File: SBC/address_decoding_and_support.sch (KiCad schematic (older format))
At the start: 15 parts, among them Q1 DS1813, SW1 RESET, SW2 PANIC, U5 TL7705B, U6 PlutoDecoder, U8 74HC74, X1 8MHz

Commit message: New PCB layout is taking shape.
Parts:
- removed RN1: 3.3k, Resistor_SMD:R_Array_Convex_8x0602, symbol Device:R_Network08
- added RN1: 3.3k, Resistor_SMD:R_Array_Convex_5x1206, symbol Grotto:R_Network08_SMD
- C10, C6, C9: footprint Capacitor_SMD:C_0603_1608Metric_Pad1.05x0.95mm_HandSolder -> Capacitor_SMD:C_0805_2012Metric_Pad1.15x1.40mm_HandSolder
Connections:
- net BE: now also RN1.7 (R6)
- net RDY: now also RN1.4 (R4)
- net VCC: now also RN1.10 (common), RN1.5 (common)
- net ~IRQ: now also RN1.9 (R8)
- net ~KS: now also RN1.2 (R2)
- net ~NMI: now also RN1.8 (R7)
- net ~PWR: now also RN1.6 (R5)
- net ~RES: now also RN1.1 (R1)
- net ~SO: now also RN1.3 (R3)
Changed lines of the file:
@@
 F 0 "C6" H 3650 3700 50  0000 L CNN
 F 1 "0.1uF" H 3425 3550 50  0000 L CNN
-F 2 "Capacitor_SMD:C_0603_1608Metric_Pad1.05x0.95mm_HandSolder" H 3650 3625 50  0001 C CNN
+F 2 "Capacitor_SMD:C_0805_2012Metric_Pad1.15x1.40mm_HandSolder" H 3650 3625 50  0001 C CNN
 F 3 "" H 3650 3625 50  0001 C CNN
 	1    3650 3625
@@
 	4350 1800 4675 1800
 Wire Wire Line
-	3650 1200 3650 1025
-Wire Wire Line
 	4650 6450 4900 6450
 Wire Wire Line
@@
 Wire Wire Line
 	3750 2400 4675 2400
-$Comp
-L Device:R_Network08 RN1
-U 1 1 5D76ADD1
-P 4050 1400
-F 0 "RN1" V 3550 1325 50  0000 L CNN
-F 1 "3.3k" V 4450 1300 50  0000 L CNN
-F 2 "Resistor_SMD:R_Array_Convex_8x0602" V 4525 1400 50  0001 C CNN
-F 3 "http://www.vishay.com/docs/31509/csc.pdf" H 4050 1400 50  0001 C CNN
-	1    4050 1400
-	1    0    0    -1
-$EndComp
 Wire Wire Line
 	4675 2500 3650 2500
@@
 F 0 "C9" V 8775 800 50  0000 C CNN
 F 1 "0.1uF" V 9025 800 50  0000 C CNN
-F 2 "Capacitor_SMD:C_0603_1608Metric_Pad1.05x0.95mm_HandSolder" H 8900 800 50  0001 C CNN
+F 2 "Capacitor_SMD:C_0805_2012Metric_Pad1.15x1.40mm_HandSolder" H 8900 800 50  0001 C CNN
 F 3 "~" H 8900 800 50  0001 C CNN
 	1    8900 800
@@
 F 0 "C10" V 3775 6775 50  0000 L CNN
 F 1 "0.1uF" V 4000 6750 50  0000 L CNN
-F 2 "Capacitor_SMD:C_0603_1608Metric_Pad1.05x0.95mm_HandSolder" H 3875 6825 50  0001 C CNN
+F 2 "Capacitor_SMD:C_0805_2012Metric_Pad1.15x1.40mm_HandSolder" H 3875 6825 50  0001 C CNN
 F 3 "" H 3875 6825 50  0001 C CNN
 	1    3875 6825
@@
 	3775 6150 4050 6150
 Connection ~ 4050 6150
+$Comp
+L Grotto:R_Network08_SMD RN1
+U 1 1 5D847681
+P 4050 1400
+F 0 "RN1" V 3550 1325 50  0000 L CNN
+F 1 "3.3k" V 4450 1325 50  0000 L CNN
+F 2 "Resistor_SMD:R_Array_Convex_5x1206" V 4525 1400 50  0001 C CNN
+F 3 "https://industrial.panasonic.com/cdbs/www-data/pdf/AOC0000/AOC0000C12.pdf" H 4050 1400 50  0001 C CNN
+	1    4050 1400
+	1    0    0    -1
+$EndComp
+Wire Wire Line
+	3650 1200 3650 1025
+Wire Wire Line
+	4350 1200 3650 1200
+Connection ~ 3650 1200
 Wire Bus Line
 	7375 1025 7375 2025

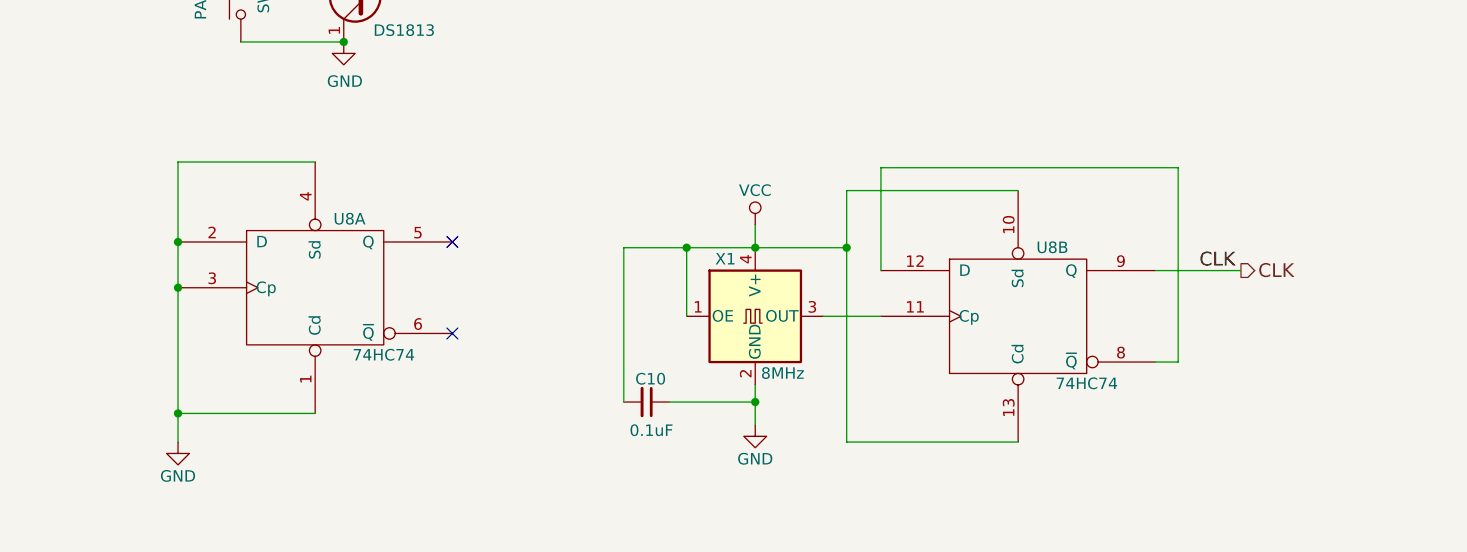
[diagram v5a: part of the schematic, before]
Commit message: Added de-coupling cap to 74hc74. Rearranged PCB a bit.
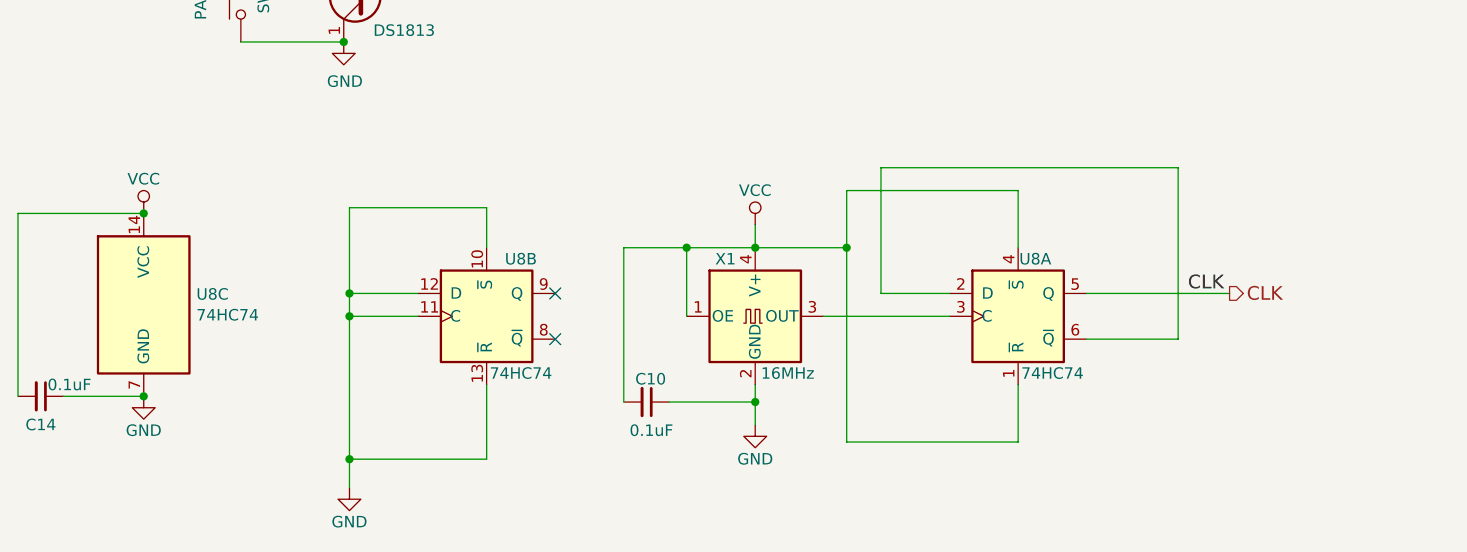
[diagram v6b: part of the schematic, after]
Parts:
- removed U8: 74HC74, Package_SO:SOIC-14_3.9x8.7mm_P1.27mm, symbol pluto-rescue:74HC74
- added C14: 0.1uF, Capacitor_SMD:C_0805_2012Metric_Pad1.15x1.40mm_HandSolder, symbol Device:C_Small
- added U8: 74HC74, Package_SO:SOIC-14_3.9x8.7mm_P1.27mm, symbol 74xx:74HC74
- C4: footprint Capacitor_Tantalum_SMD:CP_EIA-7343-31_Kemet-D_Pad2.25x2.55mm_HandSolder -> Capacitor_Tantalum_SMD:CP_EIA-3528-15_AVX-H_Pad1.50x2.35mm_HandSolder
- X1: value 8MHz -> 16MHz
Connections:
- net CLK: now also U8.5 (Q)
- net GND: now also C14.1, U8.10 (~S), U8.11 (C), U8.12 (D), U8.13 (~R), U8.7 (GND)
- net VCC: now also C14.2, U8.1 (~R), U8.14 (VCC), U8.4 (~S)
- net at X1.3 (OUT): now also U8.3 (C)
- new net: U8.2 (D), U8.6 (~Q)
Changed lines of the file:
@@
 	0    -1   -1   0
 $EndComp
-Text Label 6450 6250 2    60   ~ 0
+Text Label 6400 6350 2    60   ~ 0
 CLK
-Text HLabel 6475 6250 2    60   Output ~ 0
+Text HLabel 6425 6350 2    60   Output ~ 0
 CLK
 Text HLabel 4675 1800 2    60   BiDi ~ 0
@@
 L power:GND #PWR015
 U 1 1 595DE156
-P 1825 7000
-F 0 "#PWR015" H 1825 6750 50  0001 C CNN
-F 1 "GND" H 1825 6850 50  0000 C CNN
-F 2 "" H 1825 7000 50  0001 C CNN
-F 3 "" H 1825 7000 50  0001 C CNN
-	1    1825 7000
-	1    0    0    -1
-$EndComp
-NoConn ~ 3025 6125
-NoConn ~ 3025 6525
-$Comp
-L pluto-rescue:74HC74 U8
-U 2 1 59EC7963
-P 5500 6450
-F 0 "U8" H 5650 6750 50  0000 C CNN
-F 1 "74HC74" H 5800 6155 50  0000 C CNN
-F 2 "Package_SO:SOIC-14_3.9x8.7mm_P1.27mm" H 5500 6450 50  0001 C CNN
-F 3 "" H 5500 6450 50  0001 C CNN
-	2    5500 6450
-	1    0    0    -1
-$EndComp
-$Comp
-L pluto-rescue:74HC74 U8
-U 1 1 59EC7994
-P 2425 6325
-F 0 "U8" H 2575 6625 50  0000 C CNN
-F 1 "74HC74" H 2725 6030 50  0000 C CNN
-F 2 "Package_SO:SOIC-14_3.9x8.7mm_P1.27mm" H 2425 6325 50  0001 C CNN
-F 3 "" H 2425 6325 50  0001 C CNN
-	1    2425 6325
-	1    0    0    -1
-$EndComp
+P 2575 7200
+F 0 "#PWR015" H 2575 6950 50  0001 C CNN
+F 1 "GND" H 2575 7050 50  0000 C CNN
+F 2 "" H 2575 7200 50  0001 C CNN
+F 3 "" H 2575 7200 50  0001 C CNN
+	1    2575 7200
+	1    0    0    -1
+$EndComp
+NoConn ~ 3475 6350
+NoConn ~ 3475 6550
 $Comp
 L pluto:TL7705B U5
@@
 F 0 "C4" H 2060 4095 50  0000 L CNN
 F 1 "15uF" V 1950 3950 50  0000 L CNN
-F 2 "Capacitor_Tantalum_SMD:CP_EIA-7343-31_Kemet-D_Pad2.25x2.55mm_HandSolder" H 2050 4025 50  0001 C CNN
+F 2 "Capacitor_Tantalum_SMD:CP_EIA-3528-15_AVX-H_Pad1.50x2.35mm_HandSolder" H 2050 4025 50  0001 C CNN
 F 3 "" H 2050 4025 50  0001 C CNN
 	1    2050 4025
@@
 	4350 1800 4675 1800
 Wire Wire Line
-	4650 6450 4900 6450
+	4650 6450 5200 6450
 Wire Wire Line
 	4350 6750 4350 6825
@@
 Connection ~ 4750 6150
 Wire Wire Line
-	4900 6250 4900 5800
-Wire Wire Line
 	4900 5800 6200 5800
 Wire Wire Line
-	6200 5800 6200 6650
-Wire Wire Line
-	6200 6650 6100 6650
-Wire Wire Line
-	6100 6250 6475 6250
-Wire Wire Line
-	2425 5775 1825 5775
-Wire Wire Line
-	1825 5775 1825 6125
-Connection ~ 1825 6125
-Connection ~ 1825 6325
-Wire Wire Line
-	2425 6875 1825 6875
-Connection ~ 1825 6875
+	6200 5800 6200 6550
+Wire Wire Line
+	3175 5975 2575 5975
+Wire Wire Line
+	3175 7075 2575 7075
+Connection ~ 2575 7075
 Wire Wire Line
 	2050 3000 2050 2675
@@
 	4750 6150 4750 7000
 Wire Wire Line
-	1825 6125 1825 6325
-Wire Wire Line
-	1825 6325 1825 6875
-Wire Wire Line
-	1825 6875 1825 7000
+	2575 7075 2575 7200
 Wire Wire Line
 	2050 4125 2850 4125
@@
 P 4350 6450
 F 0 "X1" H 4175 6700 50  0000 L CNN
-F 1 "8MHz" H 4375 6200 50  0000 L CNN
+F 1 "16MHz" H 4375 6200 50  0000 L CNN
 F 2 "Oscillator:Oscillator_SMD_SeikoEpson_SG8002CA-4Pin_7.0x5.0mm" H 5050 6100 50  0001 C CNN
 F 3 "https://support.epson.biz/td/api/doc_check.php?mode=dl&lang=en&Parts=SG-8002DC" H 4250 6450 50  0001 C CNN
@@
 	4350 1200 3650 1200
 Connection ~ 3650 1200
+$Comp
+L 74xx:74HC74 U8
+U 1 1 5D9C4474
+P 5500 6450
+F 0 "U8" H 5575 6700 50  0000 C CNN
+F 1 "74HC74" H 5650 6200 50  0000 C CNN
+F 2 "Package_SO:SOIC-14_3.9x8.7mm_P1.27mm" H 5500 6450 50  0001 C CNN
+F 3 "74xx/74hc_hct74.pdf" H 5500 6450 50  0001 C CNN
+	1    5500 6450
+	1    0    0    -1
+$EndComp
+$Comp
+L 74xx:74HC74 U8
+U 2 1 5D9C4CD2
+P 3175 6450
+F 0 "U8" H 3325 6700 50  0000 C CNN
+F 1 "74HC74" H 3325 6200 50  0000 C CNN
+F 2 "Package_SO:SOIC-14_3.9x8.7mm_P1.27mm" H 3175 6450 50  0001 C CNN
+F 3 "74xx/74hc_hct74.pdf" H 3175 6450 50  0001 C CNN
+	2    3175 6450
+	1    0    0    -1
+$EndComp
+$Comp
+L 74xx:74HC74 U8
+U 3 1 5D9C5532
+P 1675 6400
+F 0 "U8" H 1905 6446 50  0000 L CNN
+F 1 "74HC74" H 1905 6355 50  0000 L CNN
+F 2 "Package_SO:SOIC-14_3.9x8.7mm_P1.27mm" H 1675 6400 50  0001 C CNN
+F 3 "74xx/74hc_hct74.pdf" H 1675 6400 50  0001 C CNN
+	3    1675 6400
+	1    0    0    -1
+$EndComp
+Wire Wire Line
+	2575 5975 2575 6350
+Wire Wire Line
+	5500 5900 5500 6150
+Wire Wire Line
+	5500 6750 5500 7000
+Wire Wire Line
+	5800 6550 6200 6550
+Wire Wire Line
+	5800 6350 6425 6350
+Wire Wire Line
+	4900 6350 5200 6350
+Wire Wire Line
+	4900 5800 4900 6350
+Wire Wire Line
+	3175 7075 3175 6750
+Wire Wire Line
+	3175 5975 3175 6150
+Wire Wire Line
+	2875 6350 2575 6350
+Connection ~ 2575 6350
+Wire Wire Line
+	2575 6350 2575 6450
+Wire Wire Line
+	2875 6450 2575 6450
+Connection ~ 2575 6450
+Wire Wire Line
+	2575 6450 2575 7075
+$Comp
+L Device:C_Small C14
+U 1 1 5DA1AC0E
+P 1225 6800
+F 0 "C14" V 1350 6800 50  0000 C CNN
+F 1 "0.1uF" V 1175 6925 50  0000 C CNN
+F 2 "Capacitor_SMD:C_0805_2012Metric_Pad1.15x1.40mm_HandSolder" H 1225 6800 50  0001 C CNN
+F 3 "~" H 1225 6800 50  0001 C CNN
+	1    1225 6800
+	0    1    1    0
+$EndComp
+Wire Wire Line
+	1675 6800 1325 6800
+Wire Wire Line
+	1125 6800 1125 6000
+Wire Wire Line
+	1125 6000 1675 6000
 Wire Bus Line
 	7375 1025 7375 2025
+$Comp
+L power:GND #PWR0102
+U 1 1 5DA2AC52
+P 1675 6800
+F 0 "#PWR0102" H 1675 6550 50  0001 C CNN
+F 1 "GND" H 1675 6650 50  0000 C CNN
+F 2 "" H 1675 6800 50  0001 C CNN
+F 3 "" H 1675 6800 50  0001 C CNN
+	1    1675 6800
+	1    0    0    -1
+$EndComp
+Connection ~ 1675 6800
+$Comp
+L power:VCC #PWR0103
+U 1 1 5DA2B8D6
+P 1675 6000
+F 0 "#PWR0103" H 1675 5850 50  0001 C CNN
+F 1 "VCC" H 1675 6150 50  0000 C CNN
+F 2 "" H 1675 6000 50  0001 C CNN
+F 3 "" H 1675 6000 50  0001 C CNN
+	1    1675 6000
+	1    0    0    -1
+$EndComp
+Connection ~ 1675 6000
 $EndSCHEMATC
